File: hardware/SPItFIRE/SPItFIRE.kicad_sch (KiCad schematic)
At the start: 0 parts

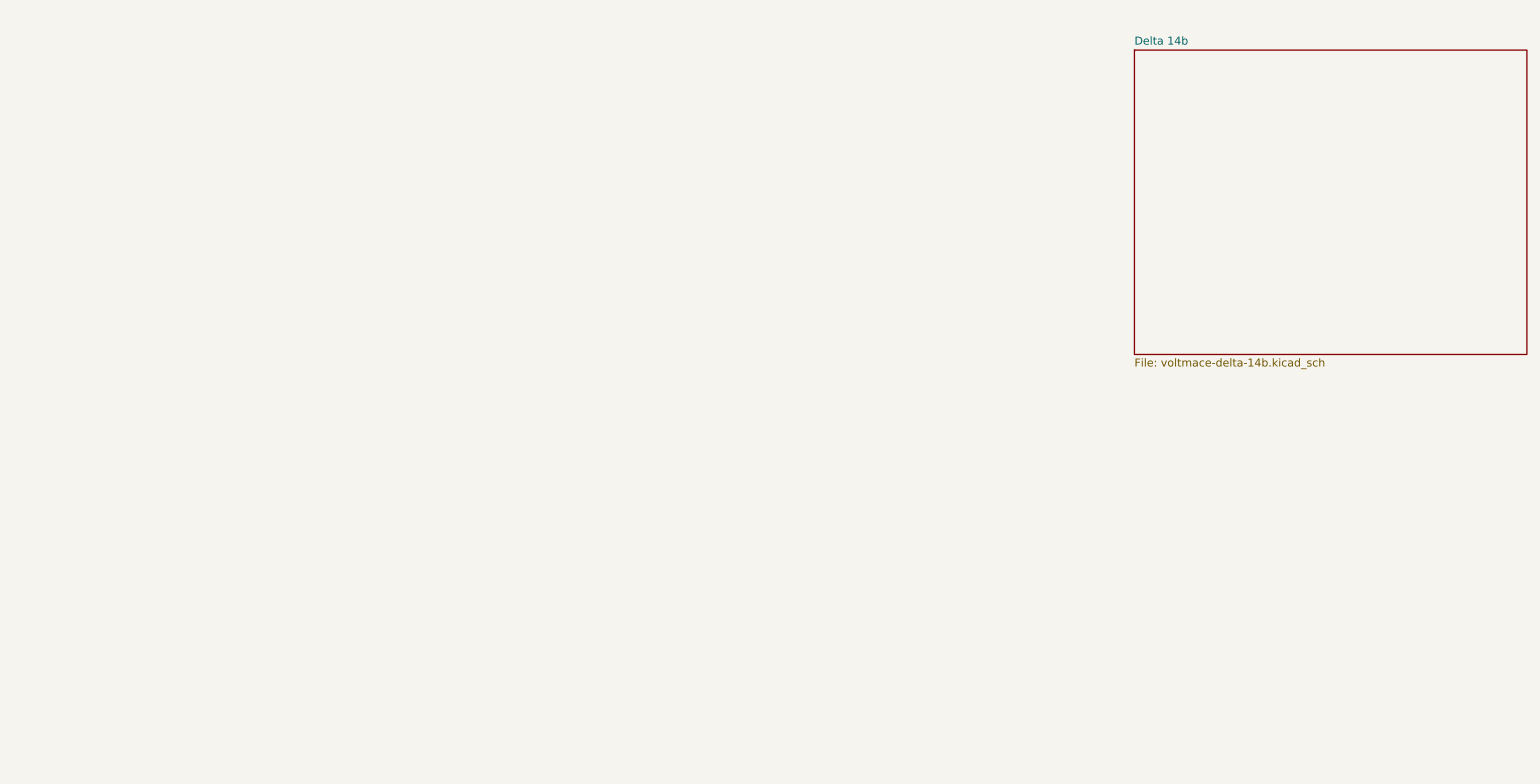
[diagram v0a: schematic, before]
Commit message: Voltmace pinouts
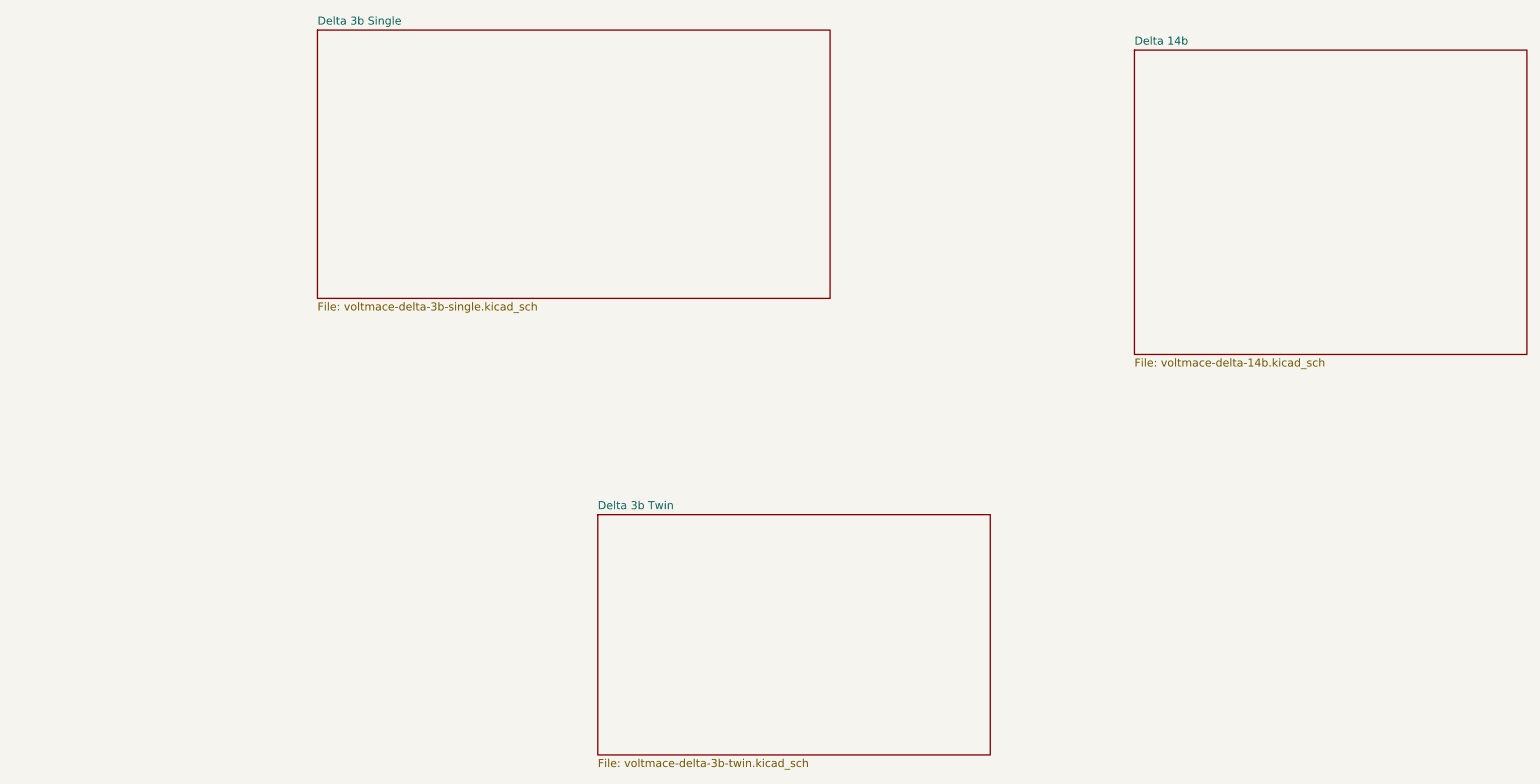
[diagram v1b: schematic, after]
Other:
- added sheet Delta 3b Single (voltmace-delta-3b-single.kicad_sch)
- added sheet Delta 3b Twin (voltmace-delta-3b-twin.kicad_sch)
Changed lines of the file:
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@@
 	(paper "A4")
+	(sheet
+		(at 74.93 26.035)
+		(size 81.28 42.545)
+		(exclude_from_sim no)
+		(in_bom yes)
+		(on_board yes)
+		(dnp no)
+		(fields_autoplaced yes)
+		(stroke
+			(width 0.1524)
+			(type solid)
+		)
+		(fill
+			(color 0 0 0 0.0000)
+		)
+		(property "Sheetname" "Delta 3b Single"
+			(at 74.93 25.3234 0)
+			(effects
+				(font
+					(size 1.27 1.27)
+				)
+				(justify left bottom)
+			)
+		)
+		(property "Sheetfile" "voltmace-delta-3b-single.kicad_sch"
+			(at 74.93 69.1646 0)
+			(effects
+				(font
+					(size 1.27 1.27)
+				)
+				(justify left top)
+			)
+		)
+		(instances
+			(project "SPItFIRE"
+				(path "/148e0ceb-efca-48fe-9d35-9803ba402dc8"
+					(page "4")
+				)
+			)
+		)
+	)
+	(sheet
+		(at 119.38 102.87)
+		(size 62.23 38.1)
+		(exclude_from_sim no)
+		(in_bom yes)
+		(on_board yes)
+		(dnp no)
+		(fields_autoplaced yes)
+		(stroke
+			(width 0.1524)
+			(type solid)
+		)
+		(fill
+			(color 0 0 0 0.0000)
+		)
+		(property "Sheetname" "Delta 3b Twin"
+			(at 119.38 102.1584 0)
+			(effects
+				(font
+					(size 1.27 1.27)
+				)
+				(justify left bottom)
+			)
+		)
+		(property "Sheetfile" "voltmace-delta-3b-twin.kicad_sch"
+			(at 119.38 141.5546 0)
+			(effects
+				(font
+					(size 1.27 1.27)
+				)
+				(justify left top)
+			)
+		)
+		(instances
+			(project "SPItFIRE"
+				(path "/148e0ceb-efca-48fe-9d35-9803ba402dc8"
+					(page "3")
+				)
+			)
+		)
+	)
 	(sheet
 		(at 204.47 29.21)

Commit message: The bulk of the schematic layout for the board (pending review and check)
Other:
- added sheet main (main.kicad_sch)
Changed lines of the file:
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@@
 (kicad_sch
-	(version 20250114)
+	(version 20260306)
 	(generator "eeschema")
-	(generator_version "9.0")
+	(generator_version "10.0")
 	(paper "A4")
 	(sheet
@@
 		)
 		(fill
-			(color 0 0 0 0.0000)
+			(color 0 0 0 0)
 		)
 		(property "Sheetname" "Delta 3b Single"
 			(at 74.93 25.3234 0)
+			(show_name no)
+			(do_not_autoplace no)
 			(effects
 				(font
@@
 		(property "Sheetfile" "voltmace-delta-3b-single.kicad_sch"
 			(at 74.93 69.1646 0)
+			(show_name no)
+			(do_not_autoplace no)
 			(effects
 				(font
@@
 				(path "/148e0ceb-efca-48fe-9d35-9803ba402dc8"
 					(page "4")
+				)
+			)
+		)
+	)
+	(sheet
+		(at 26.67 86.36)
+		(size 63.5 46.99)
+		(exclude_from_sim no)
+		(in_bom yes)
+		(on_board yes)
+		(dnp no)
+		(fields_autoplaced yes)
+		(stroke
+			(width 0.1524)
+			(type solid)
+		)
+		(fill
+			(color 0 0 0 0)
+		)
+		(property "Sheetname" "main"
+			(at 26.67 85.6484 0)
+			(show_name no)
+			(do_not_autoplace no)
+			(effects
+				(font
+					(size 1.27 1.27)
+				)
+				(justify left bottom)
+			)
+		)
+		(property "Sheetfile" "main.kicad_sch"
+			(at 26.67 133.9346 0)
+			(show_name no)
+			(do_not_autoplace no)
+			(effects
+				(font
+					(size 1.27 1.27)
+				)
+				(justify left top)
+			)
+		)
+		(instances
+			(project "SPItFIRE"
+				(path "/148e0ceb-efca-48fe-9d35-9803ba402dc8"
+					(page "5")
 				)
 			)
@@
 		)
 		(fill
-			(color 0 0 0 0.0000)
+			(color 0 0 0 0)
 		)
 		(property "Sheetname" "Delta 3b Twin"
 			(at 119.38 102.1584 0)
+			(show_name no)
+			(do_not_autoplace no)
 			(effects
 				(font
@@
 		(property "Sheetfile" "voltmace-delta-3b-twin.kicad_sch"
 			(at 119.38 141.5546 0)
+			(show_name no)
+			(do_not_autoplace no)
 			(effects
 				(font
@@
 		)
 		(fill
-			(color 0 0 0 0.0000)
+			(color 0 0 0 0)
 		)
 		(property "Sheetname" "Delta 14b"
 			(at 204.47 28.4984 0)
+			(show_name no)
+			(do_not_autoplace no)
 			(effects
 				(font
@@
 		(property "Sheetfile" "voltmace-delta-14b.kicad_sch"
 			(at 204.47 78.0546 0)
+			(show_name no)
+			(do_not_autoplace no)
 			(effects
 				(font
